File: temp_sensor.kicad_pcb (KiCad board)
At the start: 2 copper layers, 42 parts, among them J1 Conn_ARM_JTAG_SWD_10, J3 Conn_01x02_Pin, P1 USB_C_Plug_USB2.0, Q1 AO3401A, Q2 AO3400A, SW1 SW_Push, SW2 SW_Push, U1 nRF52840, U2 MCP73831-2-OT, U4 TMP112xxDRL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

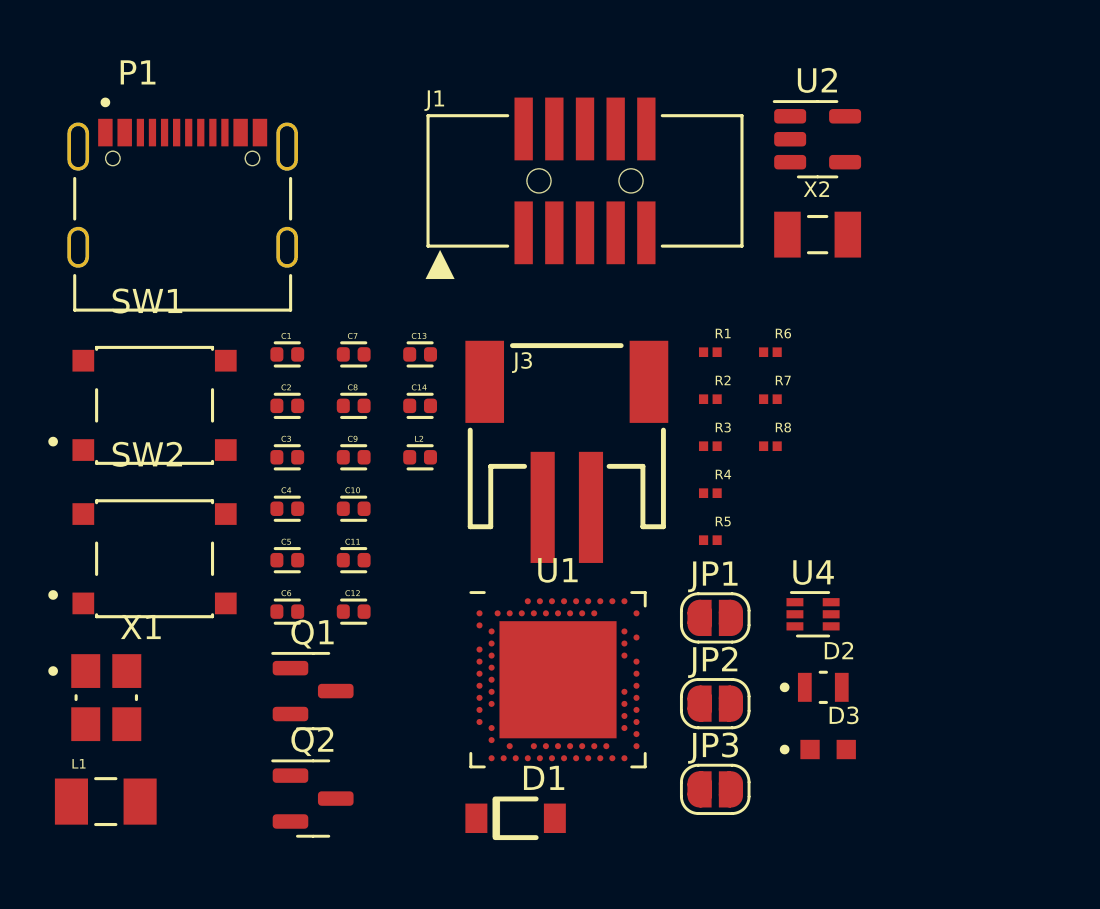
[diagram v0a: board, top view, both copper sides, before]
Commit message: Including report generated when added components to PCB
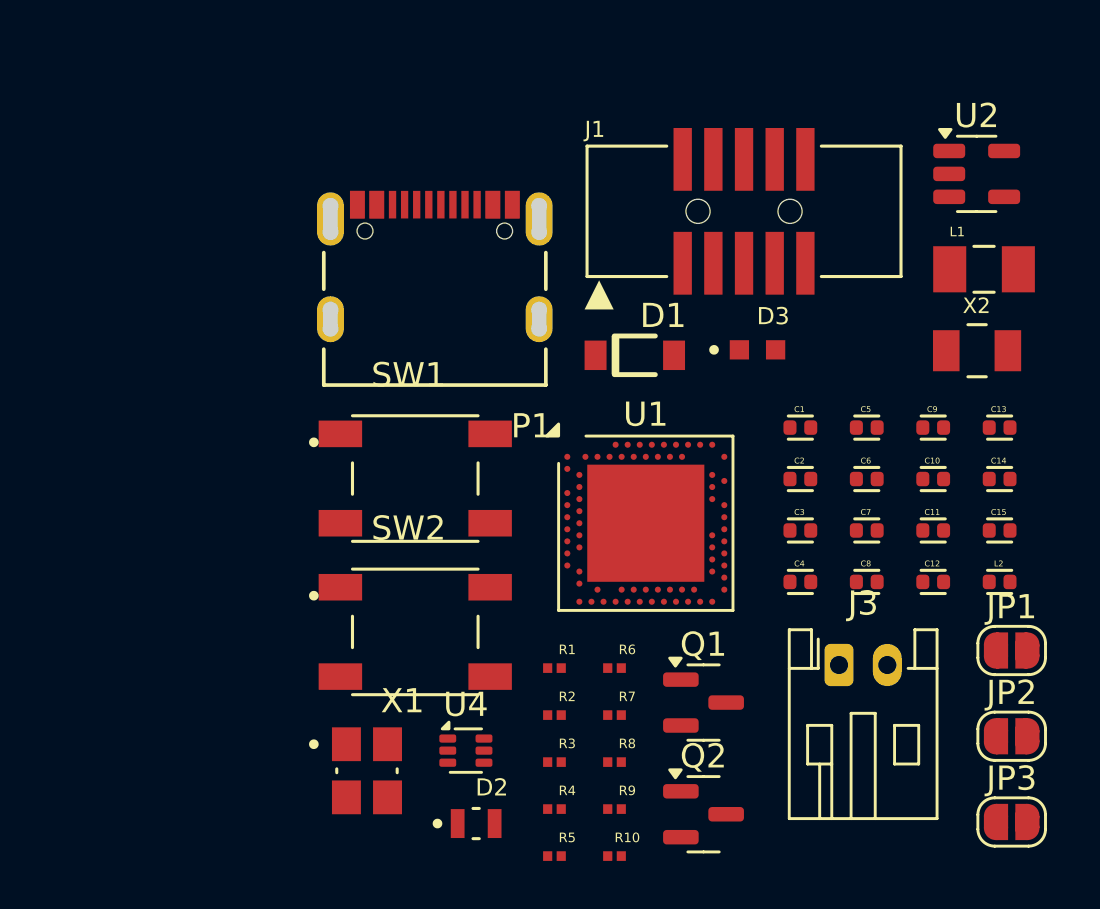
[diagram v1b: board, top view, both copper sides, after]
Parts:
- added C15: 4.7uF, custom_jlc_parts:0402_cap, F.Cu at (156.3, 94.4)
- added R10: 5.1k, custom_jlc_parts:0603_res, F.Cu at (140.4, 107.9)
- added R9: 5.1k, custom_jlc_parts:0603_res, F.Cu at (140.4, 106.0)
- J1: footprint Adafruit_nRF52840_feather:2X05_1.27MM_BOX_POSTS -> custom_jlc_parts:Adafruit_JTAG_2X05_1.27MM_BOX_POSTS
- J3: footprint Adafruit_nRF52840_feather:JSTPH2 -> Connector_JST:JST_PH_S2B-PH-K_1x02_P2.00mm_Horizontal
- P1: footprint custom_jlc_parts:usbc -> custom_jlc_parts:USBC_custom
- SW1, SW2: footprint custom_jlc_parts:switch_tactile -> custom_jlc_parts:switch_modify
- moved L1 42.5 mm to (155.7, 83.6)
- moved C5 24.6 mm to (150.8, 90.2)
- moved C6 24.6 mm to (150.8, 92.3)
- moved L2 24.5 mm to (156.3, 96.6)
- moved C13 24.2 mm to (156.3, 90.2)
- moved C14 24.2 mm to (156.3, 92.3)
- moved C10 24.0 mm to (153.6, 92.3)
- moved C11 24.0 mm to (153.6, 94.4)
- moved C12 24.0 mm to (153.6, 96.6)
- moved C9 24.0 mm to (153.6, 90.2)
- moved C7 22.5 mm to (150.8, 94.4)
- moved C8 22.5 mm to (150.8, 96.6)
- moved C1 21.5 mm to (148.1, 90.2)
- moved C2 21.5 mm to (148.1, 92.3)
- moved C3 21.5 mm to (148.1, 94.4)
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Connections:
- J1 pad 10: unconnected-(J1-~{RESET}-Pad10) -> /RESET
- J1 pad 7: unconnected-(J1-KEY-Pad7) -> GND
- SW1 pad 3: (no net) -> /RESET
- SW1 pad 4: (no net) -> GND
- SW2 pad 3: (no net) -> /SWITCH
- SW2 pad 4: (no net) -> GND
- X1 pad 2: Net-(U1-XC2) -> GND
- X1 pad 3: (no net) -> Net-(U1-XC2)
- X1 pad 4: (no net) -> GND
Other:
- board outline added: 8.6 x 5.1 mm
